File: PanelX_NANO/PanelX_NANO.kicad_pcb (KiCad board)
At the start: 2 copper layers, 95.8 x 26.5 mm, 36 parts, among them J201 Conn_01x04_Male, J202 Conn_01x04_Female, J301 RJ12, J401 Conn_02x08_Counter_Clockwise, U301 MAX485E, U601 L78L05_SOT89, U701 ATmega328-A, U702 HEADER_3x2, Y701 crystal_arduino

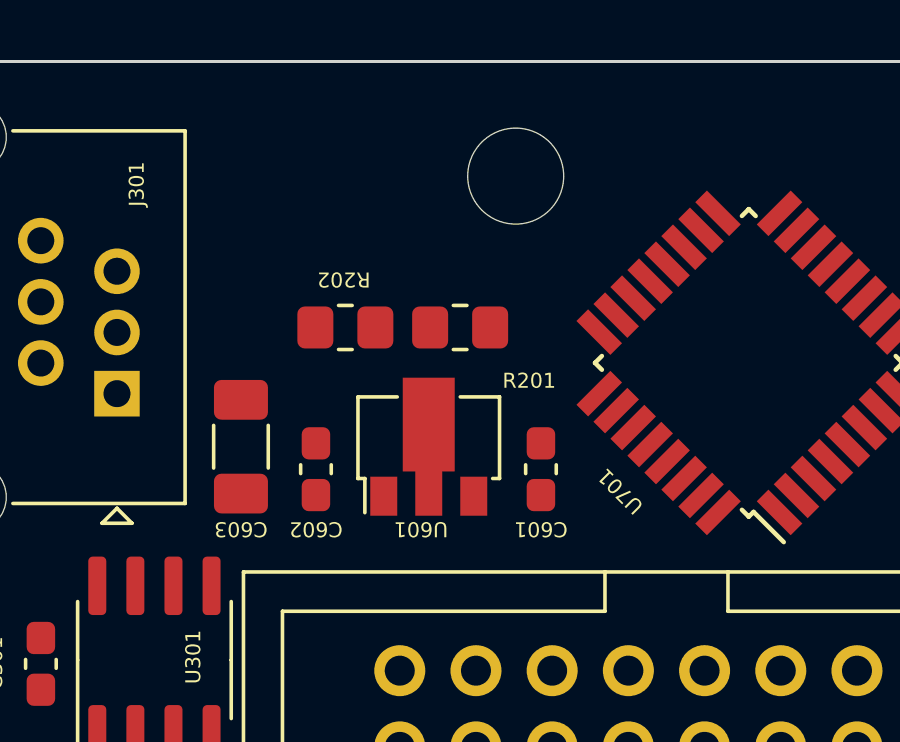
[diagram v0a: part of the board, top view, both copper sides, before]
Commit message: Deleted zip files from repo
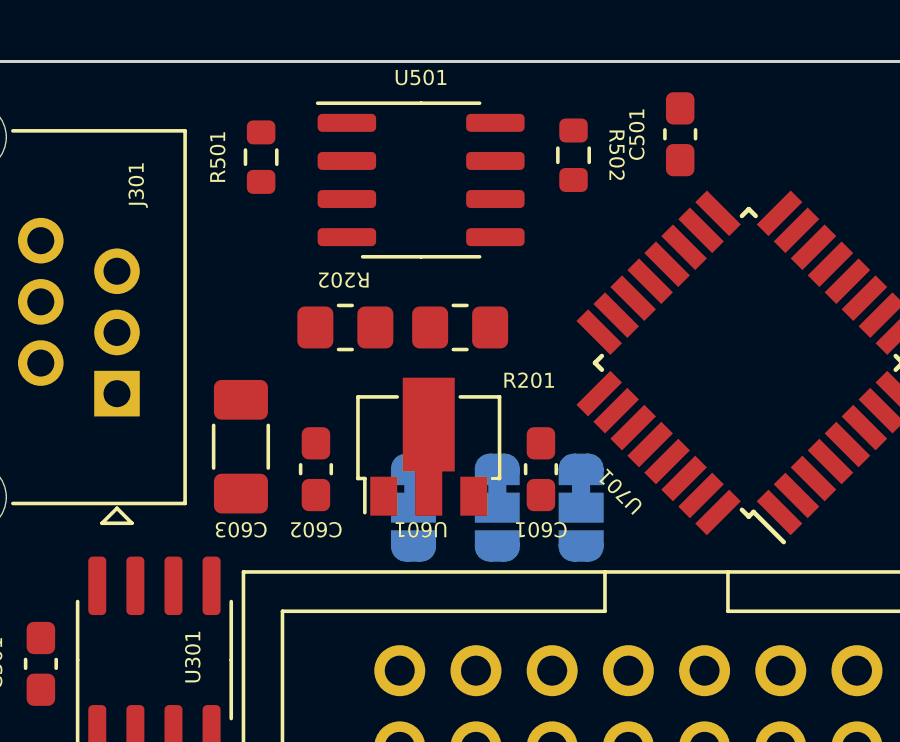
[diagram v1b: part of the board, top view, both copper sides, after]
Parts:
- removed the REF** at (120.5, 87.5)
- added C501: 100nF, Capacitor_SMD:C_0603_1608Metric_Pad1.08x0.95mm_HandSolder, F.Cu at (126.0, 86.1)
- added JP501: SolderJumper_3_Bridged12, Jumper:SolderJumper-3_P1.3mm_Bridged12_RoundedPad1.0x1.5mm_NumberLabels, B.Cu at (122.7, 98.6)
- added JP502: SolderJumper_3_Bridged12, Jumper:SolderJumper-3_P1.3mm_Bridged12_RoundedPad1.0x1.5mm_NumberLabels, B.Cu at (119.9, 98.6)
- added JP503: SolderJumper_3_Bridged12, Jumper:SolderJumper-3_P1.3mm_Bridged12_RoundedPad1.0x1.5mm_NumberLabels, B.Cu at (117.1, 98.6)
- added R501: 4k7, Resistor_SMD:R_0603_1608Metric, F.Cu at (112.0, 86.9)
- added R502: 4k7, Resistor_SMD:R_0603_1608Metric, F.Cu at (122.4, 86.8)
- added U501: 24LC256, Package_SO:SOIC-8_3.9x4.9mm_P1.27mm, F.Cu at (117.3, 87.6)

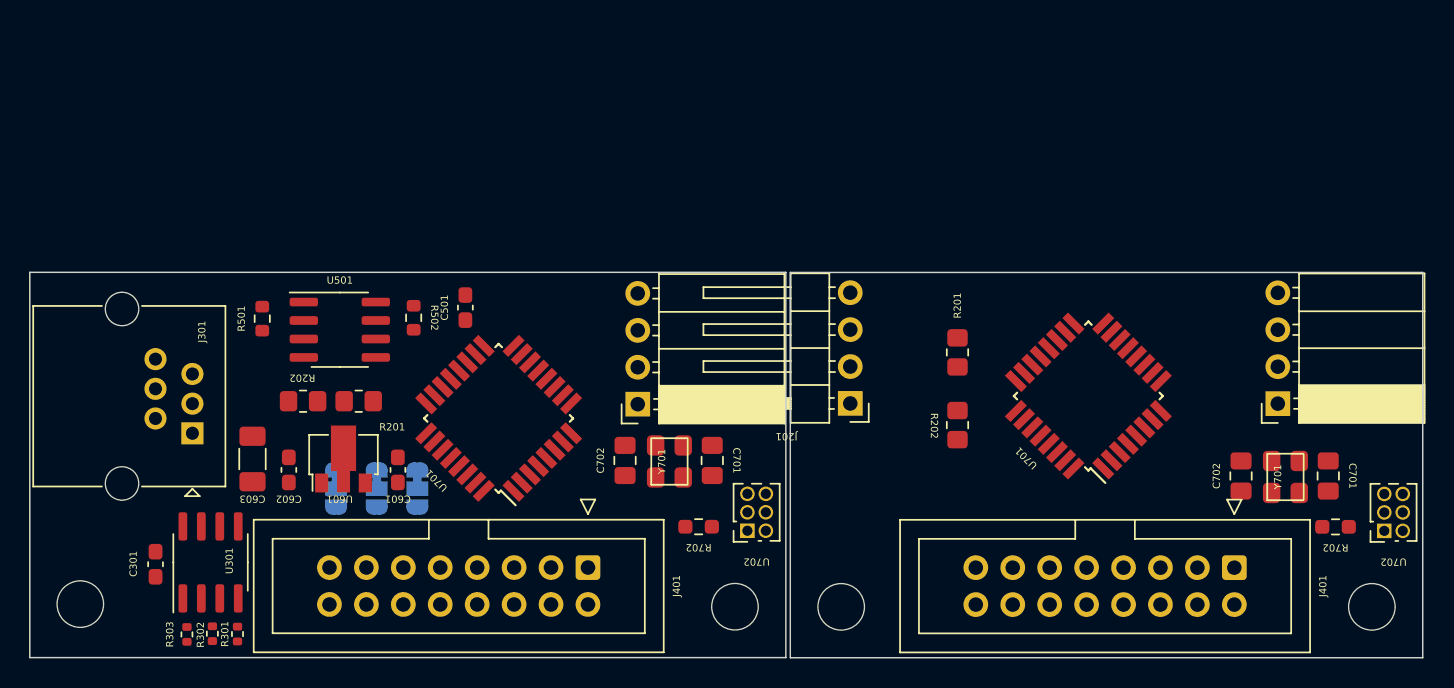
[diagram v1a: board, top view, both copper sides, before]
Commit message: I picked a suitable connector. I will use plain 2x12 female n male connectors for the b2b connector. Death to flatcables! The RJ12 connector still goed on the panel carrier board. I will look for vertical SMD variant
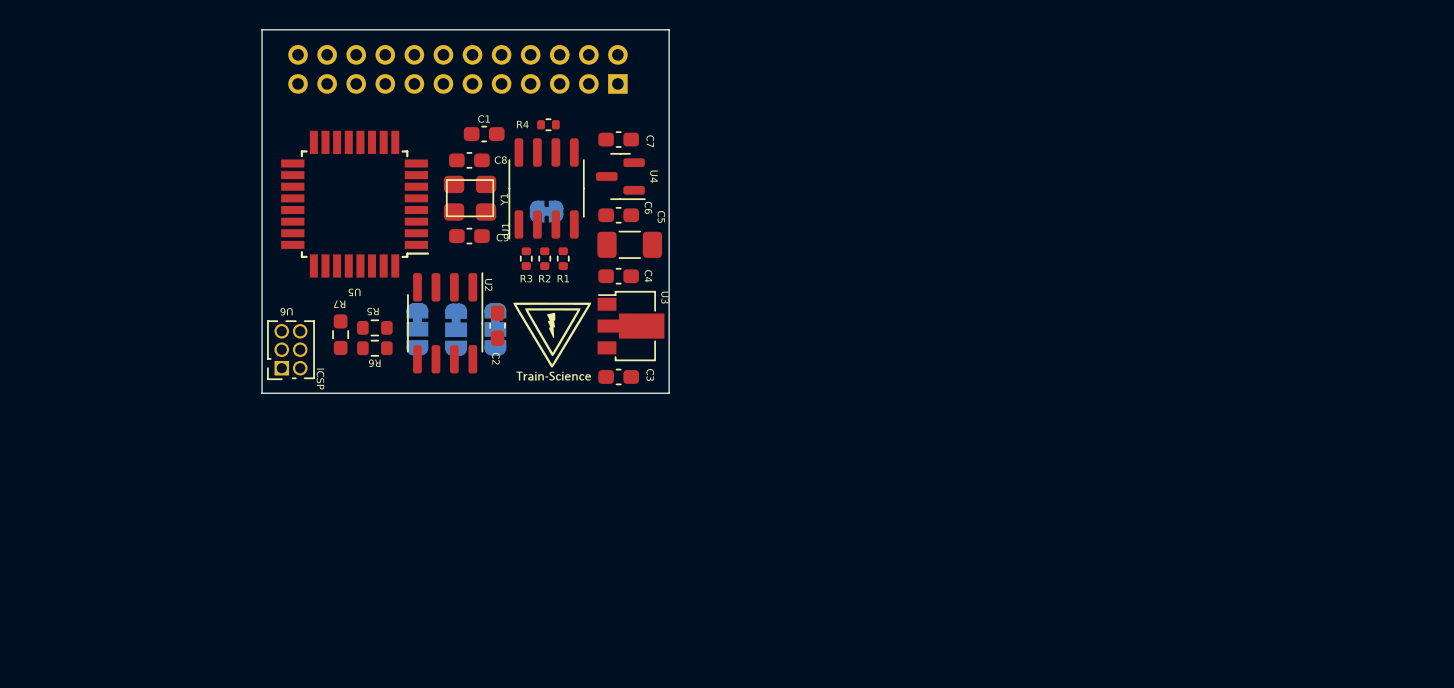
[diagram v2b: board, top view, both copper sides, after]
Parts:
- removed C301: 100n, Capacitor_SMD:C_0603_1608Metric_Pad1.08x0.95mm_HandSolder
- removed C501, C602: 100nF, Capacitor_SMD:C_0603_1608Metric_Pad1.08x0.95mm_HandSolder
- removed C601: 330nF, Capacitor_SMD:C_0603_1608Metric_Pad1.08x0.95mm_HandSolder
- removed C603: 100uF, Capacitor_SMD:C_1206_3216Metric_Pad1.33x1.80mm_HandSolder
- removed C701 (x2), C702 (x2): 12pF, Capacitor_SMD:C_0805_2012Metric_Pad1.18x1.45mm_HandSolder
- removed J201: Conn_01x04_Male, Connector_PinHeader_2.54mm:PinHeader_1x04_P2.54mm_Horizontal
- removed J202 (x2): Conn_01x04_Female, Connector_PinSocket_2.54mm:PinSocket_1x04_P2.54mm_Horizontal
- removed J301: RJ12, Connector_RJ:RJ25_Wayconn_MJEA-660X1_Horizontal
- removed J401 (x2): Conn_02x08_Counter_Clockwise, Connector_IDC:IDC-Header_2x08_P2.54mm_Vertical
- removed JP501, JP502, JP503: SolderJumper_3_Bridged12, Jumper:SolderJumper-3_P1.3mm_Bridged12_RoundedPad1.0x1.5mm_NumberLabels
- removed R201 (x2): R, Resistor_SMD:R_0805_2012Metric_Pad1.20x1.40mm_HandSolder
- removed R202 (x2): 6k2, Resistor_SMD:R_0805_2012Metric_Pad1.20x1.40mm_HandSolder
- removed R301, R302, R303: 10k, Resistor_SMD:R_0402_1005Metric
- removed R501, R502: 4k7, Resistor_SMD:R_0603_1608Metric
- removed R702 (x2): 10k, Resistor_SMD:R_0603_1608Metric_Pad0.98x0.95mm_HandSolder
- removed REF** (x4): MountingHole_3.2mm_M3, MountingHole:MountingHole_3.2mm_M3
- removed U301: MAX485E, Package_SO:SOIC-8_3.9x4.9mm_P1.27mm
- removed U501: 24LC256, Package_SO:SOIC-8_3.9x4.9mm_P1.27mm
- removed U601: L78L05_SOT89, Package_TO_SOT_SMD:SOT-89-3
- removed U701 (x2): ATmega328-A, Package_QFP:TQFP-32_7x7mm_P0.8mm
- removed U702 (x2): HEADER_3x2, Connector_PinSocket_1.27mm:PinSocket_2x03_P1.27mm_Vertical
- removed Y701 (x2): crystal_arduino, custom_kicad_lib_sk:crystal_arduino
- added C1: 100n, Capacitor_SMD:C_0603_1608Metric_Pad1.08x0.95mm_HandSolder, F.Cu at (127.3, 74.2)
- added C2: 100nF, Capacitor_SMD:C_0603_1608Metric_Pad1.08x0.95mm_HandSolder, F.Cu at (128.2, 87.3)
- added C3: 330nF, Capacitor_SMD:C_0603_1608Metric_Pad1.08x0.95mm_HandSolder, F.Cu at (136.5, 90.9)
- added C4: 100nF, Capacitor_SMD:C_0603_1608Metric_Pad1.08x0.95mm_HandSolder, F.Cu at (136.5, 83.9)
- added C5: 100uF, Capacitor_SMD:C_1206_3216Metric_Pad1.33x1.80mm_HandSolder, F.Cu at (137.3, 81.8)
- added C6: 1uF, Capacitor_SMD:C_0603_1608Metric_Pad1.08x0.95mm_HandSolder, F.Cu at (136.5, 79.8)
- added C7: 1uF, Capacitor_SMD:C_0603_1608Metric_Pad1.08x0.95mm_HandSolder, F.Cu at (136.5, 74.5)
- added C8: 12pF, Capacitor_SMD:C_0603_1608Metric_Pad1.08x0.95mm_HandSolder, F.Cu at (126.3, 76.0)
- added C9: 12pF, Capacitor_SMD:C_0603_1608Metric_Pad1.08x0.95mm_HandSolder, F.Cu at (126.3, 81.2)
- added G***: LOGO, kicad_images:Train-Science logo extra small, F.Cu at (132.0, 88.5)
- added J1: Conn_02x12_Counter_Clockwise, Connector_PinHeader_2.00mm:PinHeader_2x12_P2.00mm_Vertical, B.Cu at (136.5, 70.7)
- added JP1: SolderJumper_3_Bridged12, Jumper:SolderJumper-3_P1.3mm_Bridged12_RoundedPad1.0x1.5mm_NumberLabels, B.Cu at (128.1, 87.6)
- added JP2: SolderJumper_3_Bridged12, Jumper:SolderJumper-3_P1.3mm_Bridged12_RoundedPad1.0x1.5mm_NumberLabels, B.Cu at (125.3, 87.6)
- added JP3: SolderJumper_3_Bridged12, Jumper:SolderJumper-3_P1.3mm_Bridged12_RoundedPad1.0x1.5mm_NumberLabels, B.Cu at (122.7, 87.6)
- added JP4: SolderJumper_2_Bridged, Jumper:SolderJumper-2_P1.3mm_Bridged_RoundedPad1.0x1.5mm, B.Cu at (131.6, 79.5)
- added R1: 10k, Resistor_SMD:R_0402_1005Metric, F.Cu at (132.7, 82.7)
- added R2: 10k, Resistor_SMD:R_0402_1005Metric, F.Cu at (131.4, 82.7)
- added R3: 10k, Resistor_SMD:R_0402_1005Metric, F.Cu at (130.2, 82.7)
- added R4: 120R, Resistor_SMD:R_0402_1005Metric, F.Cu at (131.7, 73.5)
- added R5: 4k7, Resistor_SMD:R_0603_1608Metric, F.Cu at (119.8, 87.5)
- added R6: 4k7, Resistor_SMD:R_0603_1608Metric, F.Cu at (119.8, 88.9)
- added R7: 10k, Resistor_SMD:R_0603_1608Metric_Pad0.98x0.95mm_HandSolder, F.Cu at (117.4, 88.0)
- added U1: MAX485E, Package_SO:SOIC-8_3.9x4.9mm_P1.27mm, F.Cu at (131.6, 77.9)
- added U2: 24LC256, Package_SO:SOIC-8_3.9x4.9mm_P1.27mm, F.Cu at (124.6, 87.2)
- added U3: L78L05_SOT89, Package_TO_SOT_SMD:SOT-89-3, F.Cu at (137.4, 87.4)
- added U4: XC6206PxxxMR, Package_TO_SOT_SMD:SOT-23, F.Cu at (136.7, 77.1)
- added U5: ATmega328-A, Package_QFP:TQFP-32_7x7mm_P0.8mm, F.Cu at (118.4, 79.0)
- added U6: HEADER_3x2, Connector_PinSocket_1.27mm:PinSocket_2x03_P1.27mm_Vertical, F.Cu at (113.4, 90.3)
- added Y1: crystal_arduino, custom_kicad_lib_sk:crystal_arduino, F.Cu at (126.4, 78.4)
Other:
- board size 95.8 x 26.5 mm -> 28 x 25 mm
- board text added: "ICSP"
